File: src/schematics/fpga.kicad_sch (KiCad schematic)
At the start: 25 parts

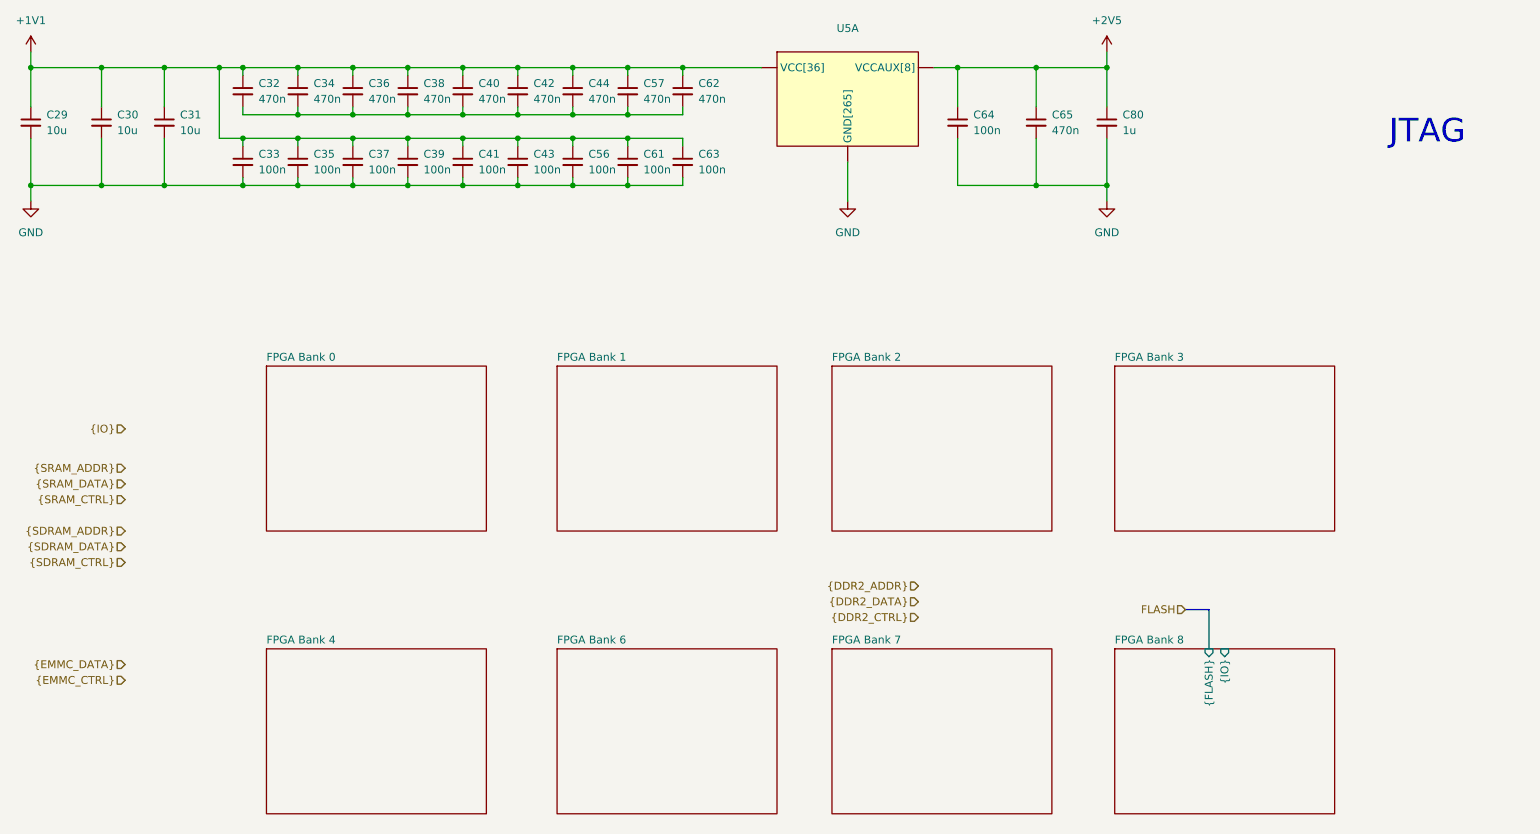
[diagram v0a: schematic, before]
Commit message: Draft connections between the FPGA and the memories
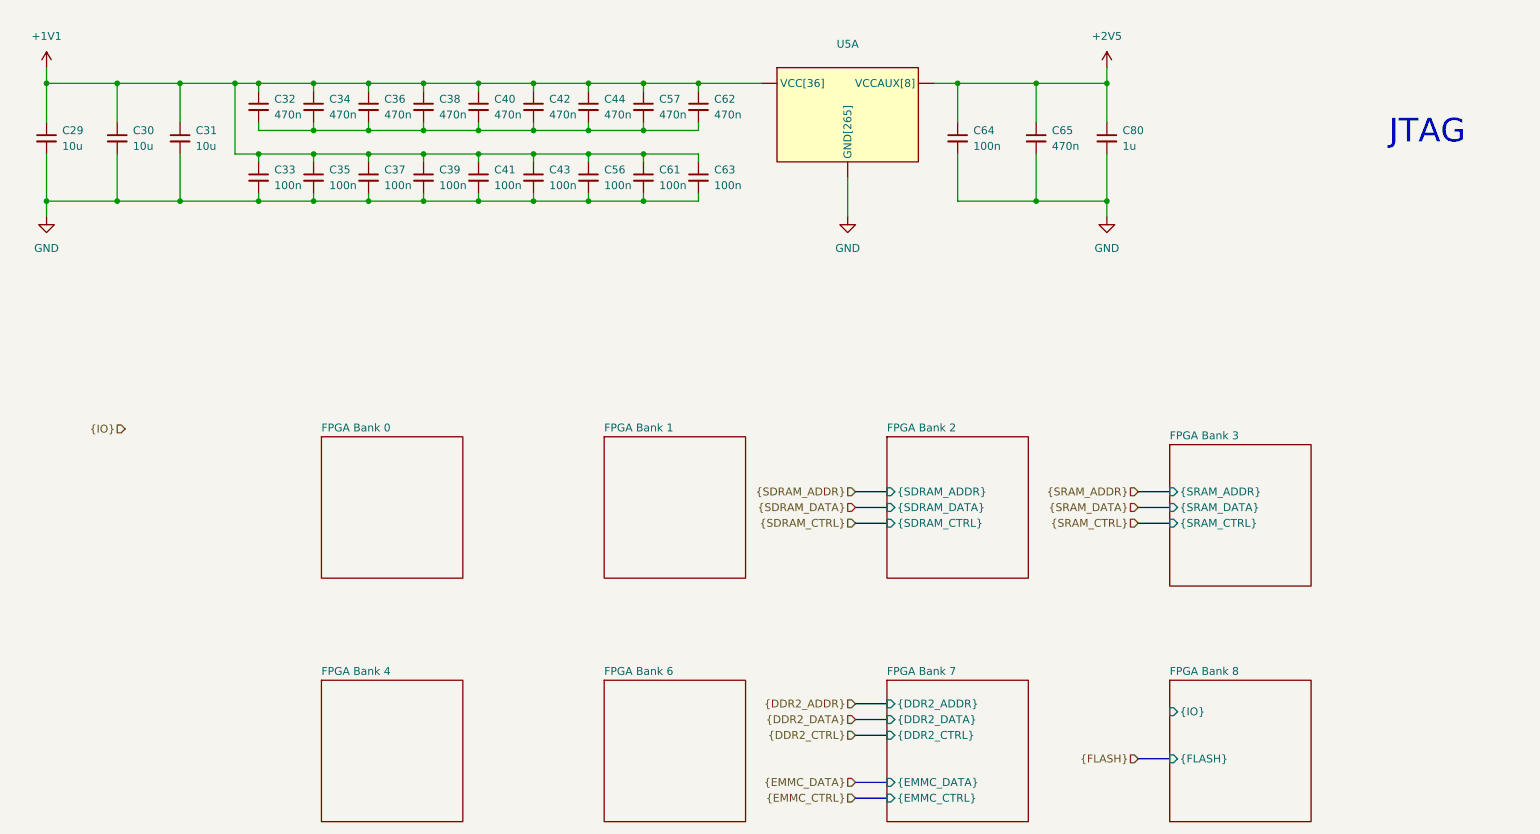
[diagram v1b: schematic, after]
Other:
- sheet FPGA Bank 2 ports: added {SDRAM_ADDR}, {SDRAM_CTRL}, {SDRAM_DATA}; removed none
- sheet FPGA Bank 3 ports: added {SRAM_ADDR}, {SRAM_CTRL}, {SRAM_DATA}; removed none
- sheet FPGA Bank 7 ports: added {DDR2_ADDR}, {DDR2_CTRL}, {DDR2_DATA}, {EMMC_CTRL}, {EMMC_DATA}; removed none
- moved on the sheet: C29, C30, C31, C32, C33, C34, C35, C36, C37, C38, C39, C40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

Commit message: Adds draft of IO connector schematic connections to FPGA
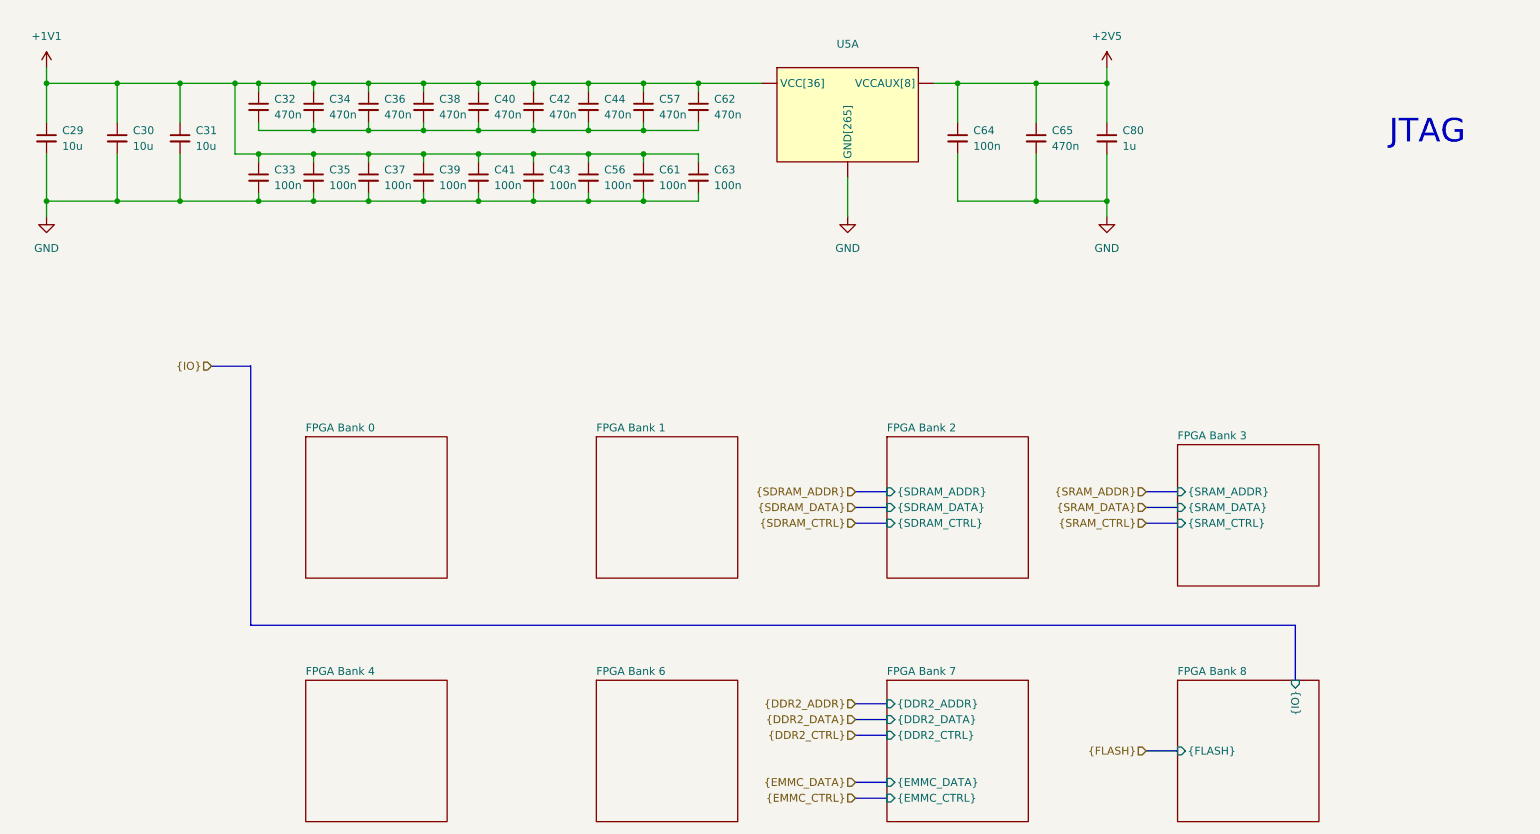
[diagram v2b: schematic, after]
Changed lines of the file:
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@@
 		)
 	)
+	(bus
+		(pts
+			(xy 60.96 121.92) (xy 229.87 121.92)
+		)
+		(stroke
+			(width 0)
+			(type default)
+		)
+	)
 	(wire
 		(pts
@@
 	(bus
 		(pts
-			(xy 204.47 100.33) (xy 209.55 100.33)
+			(xy 205.74 100.33) (xy 210.82 100.33)
 		)
 		(stroke
@@
 	(bus
 		(pts
+			(xy 229.87 121.92) (xy 229.87 130.81)
+		)
+		(stroke
+			(width 0)
+			(type default)
+		)
+	)
+	(bus
+		(pts
 			(xy 158.75 137.16) (xy 163.83 137.16)
 		)
@@
 	(bus
 		(pts
-			(xy 204.47 102.87) (xy 209.55 102.87)
+			(xy 205.74 102.87) (xy 210.82 102.87)
 		)
 		(stroke
@@
 		)
 	)
+	(bus
+		(pts
+			(xy 54.61 80.01) (xy 60.96 80.01)
+		)
+		(stroke
+			(width 0)
+			(type default)
+		)
+	)
 	(wire
 		(pts
@@
 	(bus
 		(pts
-			(xy 204.47 143.51) (xy 209.55 143.51)
+			(xy 205.74 142.24) (xy 210.82 142.24)
 		)
 		(stroke
@@
 		)
 	)
+	(bus
+		(pts
+			(xy 60.96 80.01) (xy 60.96 121.92)
+		)
+		(stroke
+			(width 0)
+			(type default)
+		)
+	)
 	(wire
 		(pts
@@
 	(bus
 		(pts
-			(xy 204.47 105.41) (xy 209.55 105.41)
+			(xy 205.74 105.41) (xy 210.82 105.41)
 		)
 		(stroke
@@
 	(hierarchical_label "{FLASH}"
 		(shape input)
-		(at 204.47 143.51 180)
+		(at 205.74 142.24 180)
 		(fields_autoplaced yes)
 		(effects
@@
 	(hierarchical_label "{SRAM_ADDR}"
 		(shape input)
-		(at 204.47 100.33 180)
+		(at 205.74 100.33 180)
 		(fields_autoplaced yes)
 		(effects
@@
 	(hierarchical_label "{SRAM_DATA}"
 		(shape input)
-		(at 204.47 102.87 180)
+		(at 205.74 102.87 180)
 		(fields_autoplaced yes)
 		(effects
@@
 	(hierarchical_label "{SRAM_CTRL}"
 		(shape input)
-		(at 204.47 105.41 180)
+		(at 205.74 105.41 180)
 		(fields_autoplaced yes)
 		(effects
@@
 	(hierarchical_label "{IO}"
 		(shape input)
-		(at 40.64 90.17 180)
+		(at 54.61 80.01 180)
 		(fields_autoplaced yes)
 		(effects
@@
 	)
 	(sheet
-		(at 209.55 130.81)
+		(at 210.82 130.81)
 		(size 22.86 22.86)
 		(fields_autoplaced yes)
@@
 		)
 		(property "Sheetname" "FPGA Bank 8"
-			(at 209.55 130.0984 0)
+			(at 210.82 130.0984 0)
 			(effects
 				(font
@@
 		)
 		(property "Sheetfile" "fpga-bank8.kicad_sch"
-			(at 209.55 154.2546 0)
+			(at 210.82 154.2546 0)
 			(effects
 				(font
@@
 		)
 		(pin "{FLASH}" input
-			(at 209.55 143.51 180)
+			(at 210.82 142.24 180)
 			(effects
 				(font
@@
 		)
 		(pin "{IO}" input
-			(at 209.55 135.89 180)
+			(at 229.87 130.81 90)
 			(effects
 				(font
 					(size 1.27 1.27)
 				)
-				(justify left)
+				(justify right)
 			)
 		)
@@
 	)
 	(sheet
-		(at 118.11 91.44)
+		(at 116.84 91.44)
 		(size 22.86 22.86)
 		(fields_autoplaced yes)
@@
 		)
 		(property "Sheetname" "FPGA Bank 1"
-			(at 118.11 90.7284 0)
+			(at 116.84 90.7284 0)
 			(effects
 				(font
@@
 		)
 		(property "Sheetfile" "fpga-bank1.kicad_sch"
-			(at 118.11 114.8846 0)
+			(at 116.84 114.8846 0)
 			(effects
 				(font
@@
 	)
 	(sheet
-		(at 118.11 130.81)
+		(at 116.84 130.81)
 		(size 22.86 22.86)
 		(fields_autoplaced yes)
@@
 		)
 		(property "Sheetname" "FPGA Bank 6"
-			(at 118.11 130.0984 0)
+			(at 116.84 130.0984 0)
 			(effects
 				(font
@@
 		)
 		(property "Sheetfile" "fpga-bank6.kicad_sch"
-			(at 118.11 154.2546 0)
+			(at 116.84 154.2546 0)
 			(effects
 				(font
@@
 	)
 	(sheet
-		(at 72.39 91.44)
+		(at 69.85 91.44)
 		(size 22.86 22.86)
 		(fields_autoplaced yes)
@@
 		)
 		(property "Sheetname" "FPGA Bank 0"
-			(at 72.39 90.7284 0)
+			(at 69.85 90.7284 0)
 			(effects
 				(font
@@
 		)
 		(property "Sheetfile" "fpga-bank0.kicad_sch"
-			(at 72.39 114.8846 0)
+			(at 69.85 114.8846 0)
 			(effects
 				(font
@@
 	)
 	(sheet
-		(at 72.39 130.81)
+		(at 69.85 130.81)
 		(size 22.86 22.86)
 		(fields_autoplaced yes)
@@
 		)
 		(property "Sheetname" "FPGA Bank 4"
-			(at 72.39 130.0984 0)
+			(at 69.85 130.0984 0)
 			(effects
 				(font
@@
 		)
 		(property "Sheetfile" "fpga-bank4.kicad_sch"
-			(at 72.39 154.2546 0)
+			(at 69.85 154.2546 0)
 			(effects
 				(font
@@
 	)
 	(sheet
-		(at 209.55 92.71)
+		(at 210.82 92.71)
 		(size 22.86 22.86)
 		(fields_autoplaced yes)
@@
 		)
 		(property "Sheetname" "FPGA Bank 3"
-			(at 209.55 91.9984 0)
+			(at 210.82 91.9984 0)
 			(effects
 				(font
@@
 		)
 		(property "Sheetfile" "fpga-bank3.kicad_sch"
-			(at 209.55 116.1546 0)
+			(at 210.82 116.1546 0)
 			(effects
 				(font
@@
 		)
 		(pin "{SRAM_CTRL}" input
-			(at 209.55 105.41 180)
+			(at 210.82 105.41 180)
 			(effects
 				(font
@@
 		)
 		(pin "{SRAM_DATA}" input
-			(at 209.55 102.87 180)
+			(at 210.82 102.87 180)
 			(effects
 				(font
@@
 		)
 		(pin "{SRAM_ADDR}" input
-			(at 209.55 100.33 180)
+			(at 210.82 100.33 180)
 			(effects
 				(font

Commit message: Adds the clock oscillator
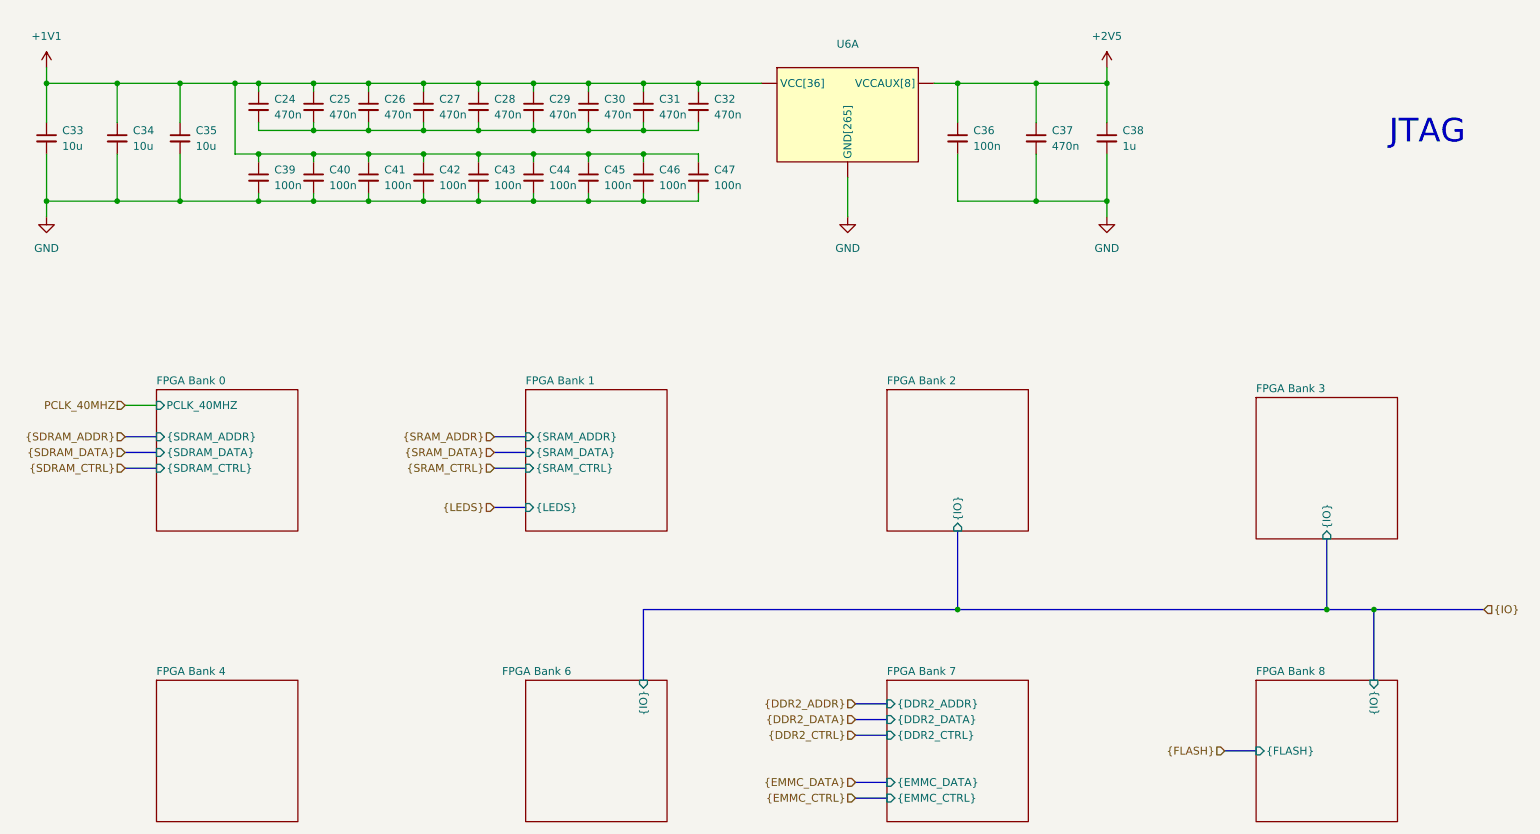
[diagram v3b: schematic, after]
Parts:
- removed U5: ~, symbol ECAP5-BSOM:LFE5U-85F-*BG756*
- added U6: ~, symbol ECAP5-BSOM:LFE5U-85F-*BG756*
- renumbered C32 to C24, C34 to C25, C36 to C26, C38 to C27, C40 to C28, C42 to C29, C44 to C30, C57 to C31, C62 to C32, C29 to C33, C30 to C34, C31 to C35, C64 to C36, C65 to C37, C80 to C38, C33 to C39, C35 to C40, C37 to C41, C39 to C42, C41 to C43, C43 to C44, C56 to C45, C61 to C46, C63 to C47
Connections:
- net +1V1: now also U6. (VCC[36]), U6.AA12 (VCC), U6.AA13 (VCC), U6.AA14 (VCC), U6.AA15 (VCC), U6.AA16 (VCC), U6.AA17 (VCC), U6.AA18 (VCC), U6.AA19 (VCC), U6.AA20 (VCC), U6.AA21 (VCC), U6.M12 (VCC), U6.M13 (VCC), U6.M14 (VCC), U6.M15 (VCC), U6.M16 (VCC), U6.M17 (VCC), U6.M18 (VCC), U6.M19 (VCC), U6.M20 (VCC), U6.M21 (VCC), U6.N12 (VCC), U6.N21 (VCC), U6.P12 (VCC), U6.P21 (VCC), U6.R12 (VCC), U6.R21 (VCC), U6.T12 (VCC), U6.T21 (VCC), U6.U12 (VCC), U6.U21 (VCC), U6.V12 (VCC), U6.V21 (VCC), U6.W12 (VCC), U6.W21 (VCC), U6.Y12 (VCC), U6.Y21 (VCC)
- net +2V5: now also U6. (VCC[36]), U6.AC11 (VCCAUX), U6.AC22 (VCCAUX), U6.K13 (VCCAUX), U6.K20 (VCCAUX), U6.N10 (VCCAUX), U6.N23 (VCCAUX), U6.Y10 (VCCAUX), U6.Y23 (VCCAUX)
- net GND: now also U6. (VCC[36]), U6.AA11 (GND), U6.AA22 (GND), U6.AB11 (GND), U6.AB12 (GND), U6.AB13 (GND), U6.AB14 (GND), U6.AB15 (GND), U6.AB16 (GND), U6.AB17 (GND), U6.AB18 (GND), U6.AB19 (GND), U6.AB20 (GND), U6.AB21 (GND), U6.AB22 (GND), U6.AC12 (GND), U6.AC13 (GND), U6.AC14 (GND), U6.AC15 (GND), U6.AC16 (GND), U6.AC17 (GND), U6.AC18 (GND), U6.AC19 (GND), U6.AC20 (GND), U6.AC21 (GND), U6.AD2 (GND), U6.AD28 (GND), U6.AD31 (GND), U6.AD5 (GND), U6.AF11 (GND), U6.AF12 (GND), U6.AF14 (GND), U6.AF15 (GND), U6.AF16 (GND), U6.AF17 (GND), U6.AF19 (GND), U6.AF20 (GND), U6.AF22 (GND), U6.AF23 (GND), U6.AG11 (GND), U6.AG12 (GND), U6.AG14 (GND), U6.AG15 (GND), U6.AG16 (GND), U6.AG17 (GND), U6.AG19 (GND), U6.AG20 (GND), U6.AG22 (GND), U6.AG23 (GND), U6.AG9 (GND), U6.AH11 (GND), U6.AH12 (GND), U6.AH14 (GND), U6.AH15 (GND), U6.AH16 (GND), U6.AH17 (GND), U6.AH19 (GND), U6.AH2 (GND), U6.AH20 (GND), U6.AH22 (GND), U6.AH23 (GND), U6.AH24 (GND), U6.AH25 (GND), U6.AH26 (GND), U6.AH29 (GND), U6.AH31 (GND), U6.AH5 (GND), U6.AH7 (GND), U6.AH8 (GND), U6.AH9 (GND), U6.AJ10 (GND), U6.AJ11 (GND), U6.AJ12 (GND), U6.AJ13 (GND), U6.AJ14 (GND), U6.AJ15 (GND), U6.AJ16 (GND), U6.AJ17 (GND), U6.AJ18 (GND), U6.AJ19 (GND), U6.AJ20 (GND), U6.AJ21 (GND), U6.AJ22 (GND), U6.AJ23 (GND), U6.AJ24 (GND), U6.AJ25 (GND), U6.AJ26 (GND), U6.AJ7 (GND), U6.AJ8 (GND), U6.AJ9 (GND), U6.AK11 (GND), U6.AK14 (GND), U6.AK17 (GND), U6.AK20 (GND), U6.AK23 (GND), U6.AK26 (GND), U6.AK7 (GND), U6.AK8 (GND), U6.AL11 (GND), U6.AL12 (GND), U6.AL14 (GND), U6.AL15 (GND), U6.AL17 (GND), U6.AL18 (GND), U6.AL2 (GND), U6.AL20 (GND), U6.AL21 (GND), U6.AL23 (GND), U6.AL24 (GND), U6.AL26 (GND), U6.AL29 (GND), U6.AL31 (GND), U6.AL5 (GND), U6.AL7 (GND), U6.AL8 (GND), U6.AL9 (GND), U6.AM11 (GND), U6.AM12 (GND), U6.AM14 (GND), U6.AM15 (GND), U6.AM17 (GND), U6.AM18 (GND), U6.AM20 (GND), U6.AM21 (GND), U6.AM23 (GND), U6.AM24 (GND), U6.AM26 (GND), U6.AM7 (GND), U6.AM8 (GND), U6.AM9 (GND), U6.B13 (GND), U6.B15 (GND), U6.B18 (GND), U6.B2 (GND), U6.B20 (GND), U6.B24 (GND), U6.B28 (GND), U6.B31 (GND), U6.B5 (GND), U6.B9 (GND), U6.E13 (GND), U6.E15 (GND), U6.E18 (GND), U6.E2 (GND), U6.E20 (GND), U6.E24 (GND), U6.E28 (GND), U6.E31 (GND), U6.E5 (GND), U6.E9 (GND), U6.J2 (GND), U6.J28 (GND), U6.J31 (GND), U6.J5 (GND), U6.K10 (GND), U6.K11 (GND), U6.K22 (GND), U6.K23 (GND), U6.L10 (GND), U6.L11 (GND), U6.L12 (GND), U6.L13 (GND), U6.L14 (GND), U6.L15 (GND), U6.L16 (GND), U6.L17 (GND), U6.L18 (GND), U6.L19 (GND), U6.L20 (GND), U6.L21 (GND), U6.L22 (GND), U6.L23 (GND), U6.M11 (GND), U6.M22 (GND), U6.N11 (GND), U6.N13 (GND), U6.N14 (GND), U6.N15 (GND), U6.N16 (GND), U6.N17 (GND), U6.N18 (GND), U6.N19 (GND), U6.N2 (GND), U6.N20 (GND), U6.N22 (GND), U6.N28 (GND), U6.N31 (GND), U6.N5 (GND), U6.P11 (GND), U6.P13 (GND), U6.P14 (GND), U6.P15 (GND), U6.P16 (GND), U6.P17 (GND), U6.P18 (GND), U6.P19 (GND), U6.P22 (GND), U6.R13 (GND), U6.R14 (GND), U6.R15 (GND), U6.R16 (GND), U6.R17 (GND), U6.R18 (GND), U6.R19 (GND), U6.R2 (GND), U6.R20 (GND), U6.R22 (GND), U6.R28 (GND), U6.R31 (GND), U6.R5 (GND), U6.T11 (GND), U6.T13 (GND), U6.T14 (GND), U6.T15 (GND), U6.T16 (GND), U6.T17 (GND), U6.T18 (GND), U6.T19 (GND), U6.T20 (GND), U6.T22 (GND), U6.U11 (GND), U6.U13 (GND), U6.U14 (GND), U6.U15 (GND), U6.U16 (GND), U6.U17 (GND), U6.U18 (GND), U6.U19 (GND), U6.U20 (GND), U6.U22 (GND), U6.V11 (GND), U6.V13 (GND), U6.V14 (GND), U6.V15 (GND), U6.V16 (GND), U6.V17 (GND), U6.V18 (GND), U6.V19 (GND), U6.V2 (GND), U6.V20 (GND), U6.V22 (GND), U6.V28 (GND), U6.V31 (GND), U6.V5 (GND), U6.W11 (GND), U6.W13 (GND), U6.W14 (GND), U6.W15 (GND), U6.W16 (GND), U6.W17 (GND), U6.W18 (GND), U6.W19 (GND), U6.W20 (GND), U6.W22 (GND), U6.Y11 (GND), U6.Y13 (GND), U6.Y14 (GND), U6.Y15 (GND), U6.Y16 (GND), U6.Y17 (GND), U6.Y18 (GND), U6.Y19 (GND), U6.Y2 (GND), U6.Y20 (GND), U6.Y22 (GND), U6.Y31 (GND)
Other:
- sheet FPGA Bank 0 ports: added PCLK_40MHZ, {SDRAM_ADDR}, {SDRAM_CTRL}, {SDRAM_DATA}; removed none
- sheet FPGA Bank 1 ports: added {LEDS}, {SRAM_ADDR}, {SRAM_CTRL}, {SRAM_DATA}; removed none
- sheet FPGA Bank 2 ports: added {IO}; removed {SDRAM_ADDR}, {SDRAM_CTRL}, {SDRAM_DATA}
- sheet FPGA Bank 3 ports: added {IO}; removed {SRAM_ADDR}, {SRAM_CTRL}, {SRAM_DATA}
- sheet FPGA Bank 6 ports: added {IO}; removed none
